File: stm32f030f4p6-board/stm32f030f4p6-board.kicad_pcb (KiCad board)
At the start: 2 copper layers, 18 parts, among them J1 SWD_Power, J2 Boot0_selector, J3 Conn_01x07_Pin, J5 Conn_01x07_Pin, SW1 MCU_reset, U1 STM32F030F4Px

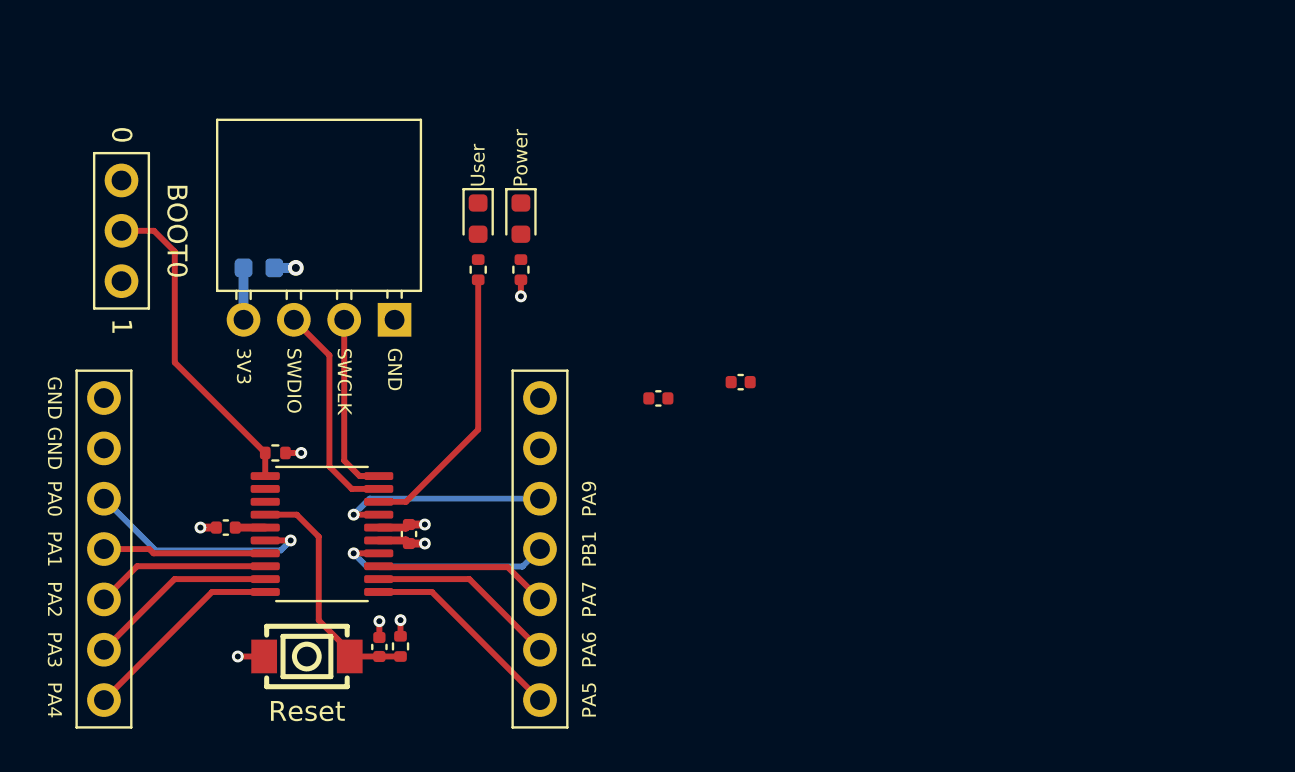
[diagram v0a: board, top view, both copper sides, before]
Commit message: final
some 3d models aren't on the PCB(I don't care :) )
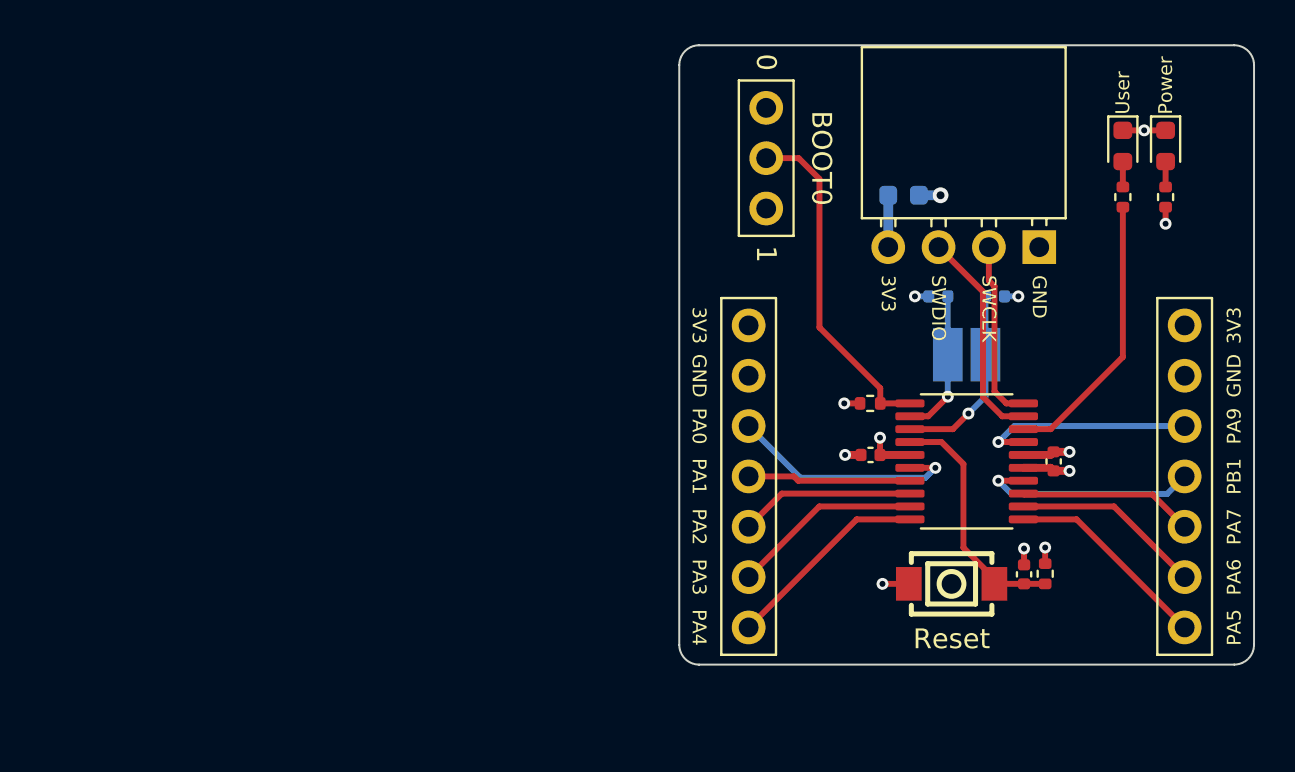
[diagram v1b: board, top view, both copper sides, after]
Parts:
- added Y1: 8Mhz, footprints:NX3225GD8MHZSTDCRA3, B.Cu at (96.5, 63.6)
- C1, C2: moved to B.Cu
- J2: footprint Connector_PinHeader_2.54mm:PinHeader_1x03_P2.54mm_Vertical -> footprints:boot0selector
- moved C6 32.7 mm to (99.4, 74.7)
- moved D2 32.7 mm to (104.4, 53.1)
- moved R3 32.7 mm to (100.5, 74.7)
- moved C4 32.7 mm to (91.6, 68.7)
- moved J5 32.7 mm to (85.5, 62.1)
- moved SW1 32.7 mm to (95.7, 75.2)
- moved U1 32.7 mm to (96.5, 69.0)
- moved C3 32.7 mm to (100.9, 69.0)
- moved C5 32.7 mm to (93.3, 55.6)
- moved D1 32.7 mm to (106.5, 53.1)
- moved J1 32.7 mm to (100.2, 58.2)
- moved J2 32.7 mm to (86.4, 56.2)
- moved J3 32.7 mm to (107.5, 62.1)
- moved R4 32.7 mm to (106.5, 55.7)
- moved R5 32.7 mm to (104.4, 55.7)
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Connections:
- J3 pad 1: unconnected-(J3-Pin_1-Pad1) -> +3.3V
- J3 pad 2: unconnected-(J3-Pin_2-Pad2) -> GND
- J5 pad 1: unconnected-(J5-Pin_1-Pad1) -> +3.3V
- J5 pad 2: unconnected-(J5-Pin_2-Pad2) -> GND
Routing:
- net Net-(U1-PF1): track 0.00 -> 9.55 mm, vias 0 -> 1
- net Net-(U1-PF0): track 0.00 -> 7.38 mm, vias 0 -> 1
- net GND: track 7.23 -> 10.8 mm, vias 6 -> 9
- net Net-(D2-A): track 0.00 -> 1.28 mm
- net Net-(D1-A): track 0.00 -> 1.28 mm
- net /boot0: track 16.3 -> 17.2 mm
- net +3.3V: track 8.17 -> 9.04 mm, vias 3 -> 4
- added copper zone on In2.Cu, net +3.3V
- added copper zone on In1.Cu, net GND
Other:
- board outline added: 29 x 31.2 mm
- copper layers 2 -> 4

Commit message: ---
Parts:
- C1, C2, C5, Y1: moved to F.Cu
- J3, J5: moved to B.Cu
- moved D1 30.5 mm to (88.0, 77.3), turned to 90 degrees
- moved R4 26.6 mm to (88.0, 74.7), turned to -90 degrees
- moved D2 24.3 mm to (105.8, 77.3), turned to 90 degrees
- moved SW1 21.8 mm to (96.9, 53.4)
- moved C6 21.6 mm to (101.6, 53.2)
- moved R3 21.5 mm to (100.5, 53.2)
- moved C5 19.7 mm to (101.5, 73.5)
- moved R5 19.1 mm to (105.8, 74.7), turned to -90 degrees
- moved J1 18.1 mm to (100.7, 76.3)
- moved J2 13.1 mm to (99.4, 57.4), turned to -90 degrees
- moved J5 5.71 mm to (88.0, 57.0), turned to 180 degrees
- moved J3 5.42 mm to (105.8, 57.0), turned to 180 degrees
- moved R1 1.79 mm to (93.1, 65.0)
- moved Y1 0.90 mm to (96.9, 62.8)
- moved C1 0.86 mm to (95.5, 59.9)
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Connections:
- J1 pad 1: GND -> +3.3V
- J1 pad 2: /SWCLK -> /SWDIO
- J1 pad 3: /SWDIO -> /SWCLK
- J1 pad 4: +3.3V -> GND
- J3 pad 3: /PA9 -> /PA10
- J3 pad 4: /PB1 -> /PA9
- J3 pad 5: /PA7 -> /PB1
- J3 pad 6: /PA6 -> /PA7
- J3 pad 7: /PA5 -> /PA6
- R5 pad 1: /PA10 -> /PA5
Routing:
- net /nrst: track 12.4 -> 21.8 mm, vias 0 -> 2
- net /boot0: track 17.2 -> 10.5 mm, vias 0 -> 1
- net /PA10: track 14.1 -> 8.49 mm
- net /PA4: track 10.4 -> 6.16 mm
- net /SWCLK: track 9.11 -> 13.0 mm
- net /PA5: track 10.4 -> 6.97 mm
- net /PA6: track 9.61 -> 6.42 mm
- net /PA3: track 9.61 -> 6.68 mm
- net /PA7: track 8.83 -> 6.41 mm
- net /PA1: track 8.23 -> 9.89 mm
- net /PB1: track 11.3 -> 9.82 mm
- net GND: track 10.8 -> 9.61 mm, vias 9 -> 10
- net Net-(U1-PF0): track 7.38 -> 8.38 mm, vias 1 -> 0
- net /SWDIO: track 10.9 -> 11.9 mm
- net /PA9: track 11.0 -> 10.1 mm
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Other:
- board size 29 x 31.2 mm -> 23 x 29.5 mm
- board text added: "CLK"
- board text added: "DIO"
- board text added: "PA10"
- board text removed: "BOOT0"
- board text removed: "PA5"
- board text removed: "Reset"
- board text removed: "SWCLK"
- board text removed: "SWDIO"
